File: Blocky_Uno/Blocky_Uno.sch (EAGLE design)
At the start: 49 parts, among them J1 10118193-0001LF, U1 1117-3.3V, U2 CH340T, U4 ATmega328mu, X1 12MHz, X2 16MHz

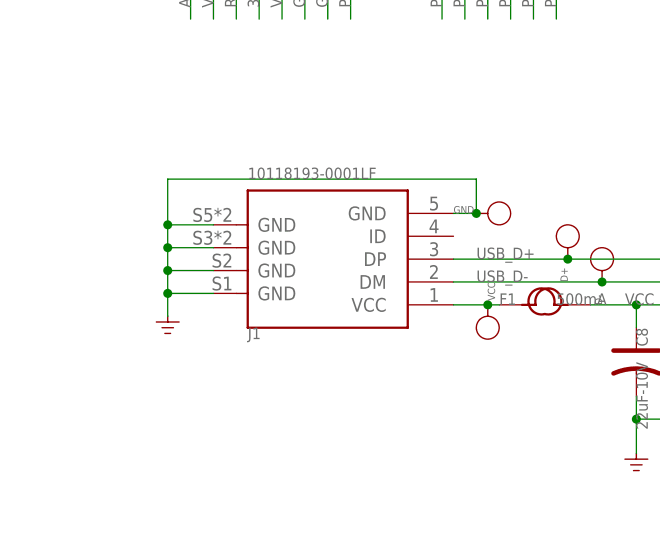
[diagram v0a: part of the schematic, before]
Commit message: Update Blocky Uno
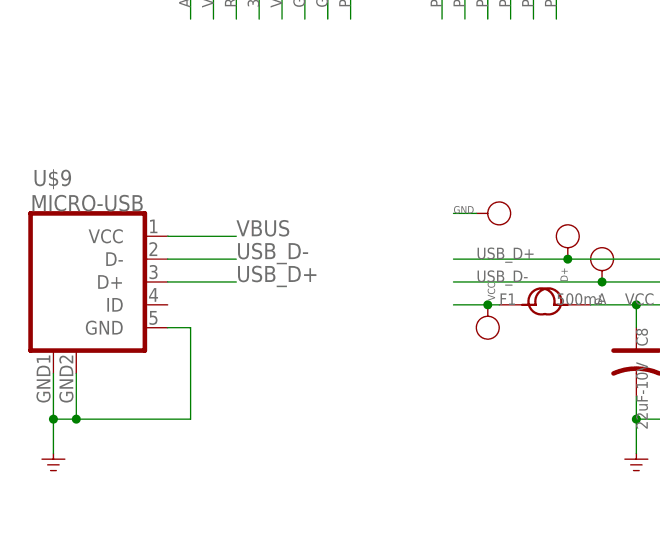
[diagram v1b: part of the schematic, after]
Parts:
- removed J1: 10118193-0001LF, Seeed-Connector -2016:MICRO-USB-SMD-B-(10118193-0001LF)
- added U$9: MICRO-USB, My-Eagle-Lib:MICRO-USB
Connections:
- removed net N$12: F1.1, J1.VCC, VCC.T
- new net VBUS: F1.1, U$9.VCC, VCC.T
- net GND: now also U$9.GND, U$9.GND@1, U$9.GND@2; no longer J1.GND@1, J1.GND@2, J1.GND@3, J1.GND@4, J1.GND@5
- net USB_D+: now also U$9.D+; no longer J1.DP
- net USB_D-: now also U$9.D-; no longer J1.DM
